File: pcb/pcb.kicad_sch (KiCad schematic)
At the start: 71 parts, among them J1 WH, J2 RGB, J3 220, Q1 AO3400A, Q2 AO3400A, Q3 AO3400A, Q4 AO3400A, Q5 AOD452, Q6 DTD114E, Q7 AO3400A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

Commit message: -0.5 cm
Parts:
- added C15: 0.1, Capacitor_THT:C_Rect_L13.0mm_W6.0mm_P10.00mm_FKS3_FKP3_MKS4, symbol Device:C_Small
- C1: footprint Capacitor_THT:CP_Radial_D13.0mm_P7.50mm -> Capacitor_THT:CP_Radial_D10.0mm_P7.50mm
- L1: footprint Inductor_THT:Choke_Schaffner_RN212-04-12.5x18.0mm -> local:Input_coil
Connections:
- net at J3.2 (Pin_2), TH1.1: no longer RV1.1
- net at J3.1 (Pin_1), R1.1: no longer RV1.2
- net at D1.3, L1.4: now also C15.2
- net at D1.4, L1.2: now also C15.1
- net at L1.1, TH1.2: now also RV1.1
- net at L1.3, R1.2: now also RV1.2
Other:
- moved on the sheet: L1, R1, RV1, TH1

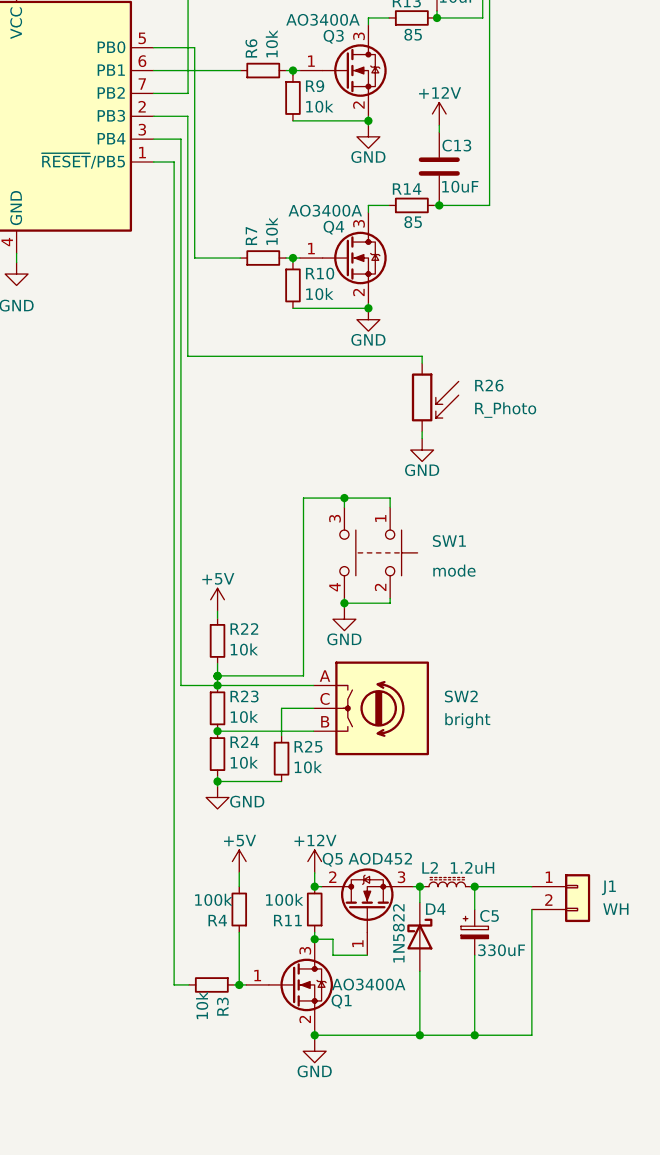
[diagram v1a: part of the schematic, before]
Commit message: mosfet bootstrap circuit
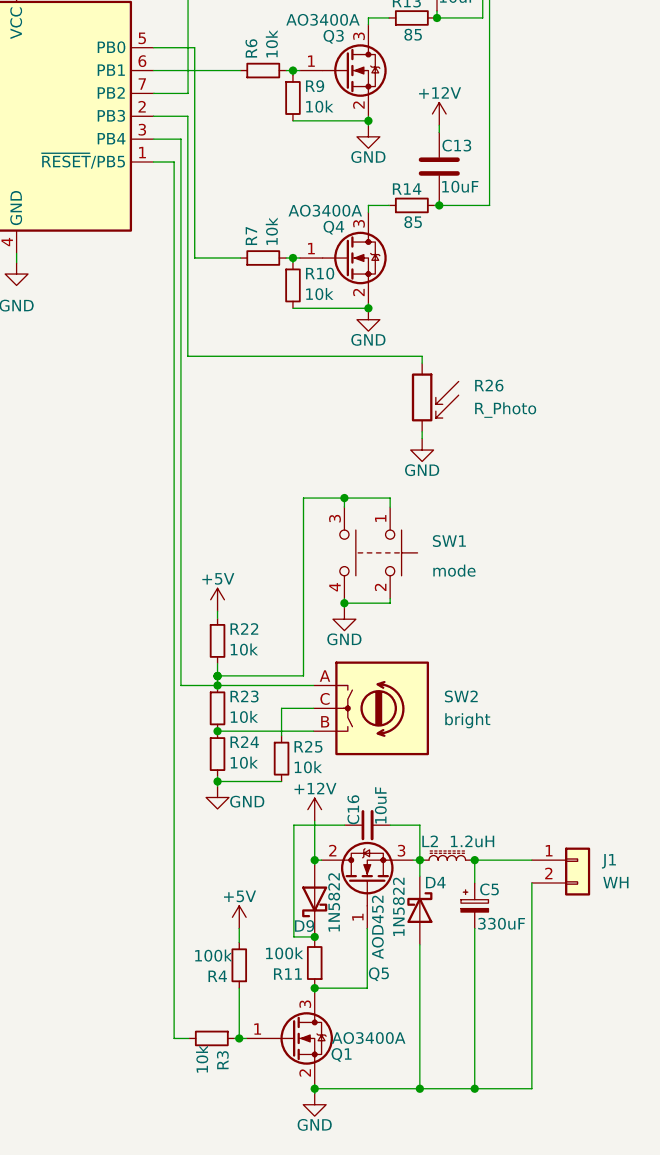
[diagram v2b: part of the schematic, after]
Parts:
- added C16: 10uF, Capacitor_SMD:C_0805_2012Metric, symbol Device:C_Small
- added D9: 1N5822, Diode_SMD:D_SOD-323, symbol Diode:1N5822
- C15: footprint Capacitor_THT:C_Rect_L13.0mm_W6.0mm_P10.00mm_FKS3_FKP3_MKS4 -> Capacitor_THT:C_Disc_D11.0mm_W5.0mm_P10.00mm
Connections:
- net +12V: now also D9.2 (A); no longer R11.2
- net at D4.1 (K), L2.1, Q5.3 (S): now also C16.2
- new net: C16.1, D9.1 (K), R11.2
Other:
- moved on the sheet: C5, D4, J1, L2, Q1, Q5, R11, R3, R4
